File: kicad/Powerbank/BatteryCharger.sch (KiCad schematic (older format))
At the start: 48 parts, among them IC4 BQ25703ARSNT, Q4 Q_NMOS_GDS, Q5 Q_NMOS_GDS, Q8 Q_PMOS_GDS

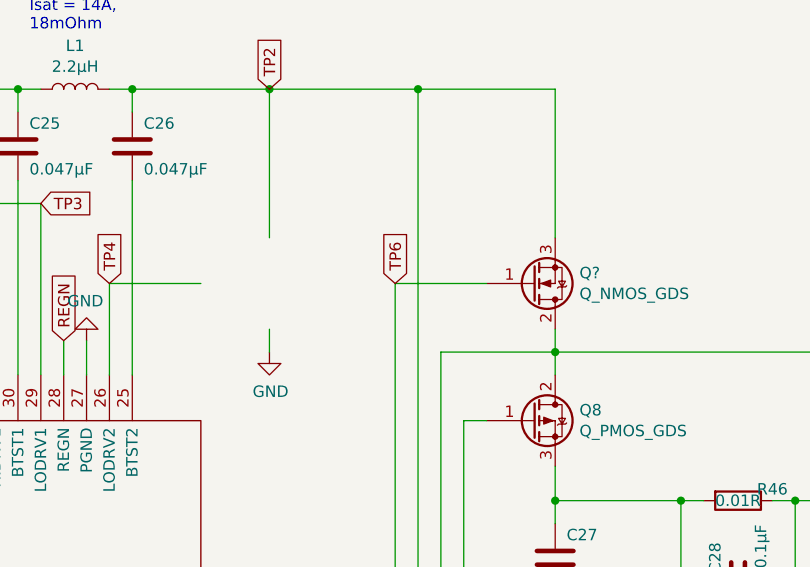
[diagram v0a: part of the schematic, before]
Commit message: Added more routing
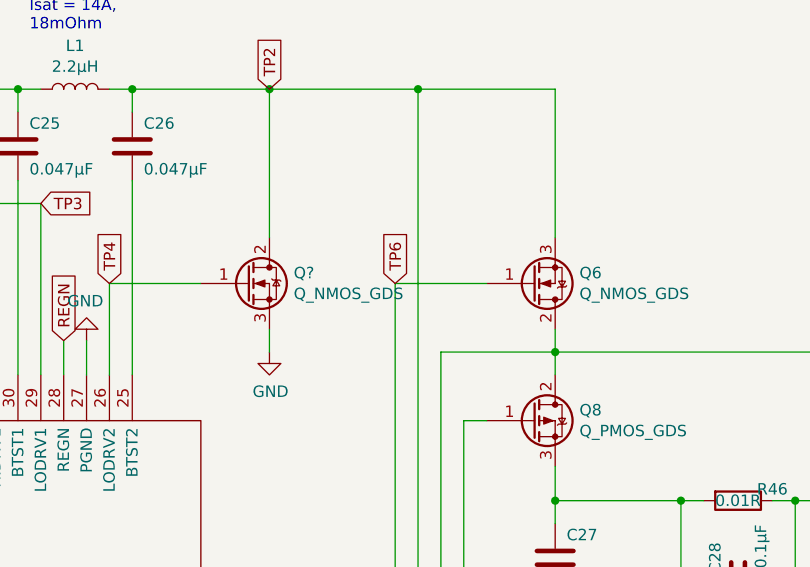
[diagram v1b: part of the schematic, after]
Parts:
- added Q?: Q_NMOS_GDS, Package_TO_SOT_SMD:TO-252-3_TabPin2, symbol Device:Q_NMOS_GDS
- gave numbers to parts that had none: 1
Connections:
- net GND: now also Q?.3 (S)
- net TP2: now also Q?.2 (D)
- net TP4: now also Q?.1 (G)
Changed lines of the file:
@@
+$EndComp
+$Comp
+L Device:Q_NMOS_GDS Q4
+U 1 1 5E148441
+P 4350 1700
+F 0 "Q4" V 4693 1700 50  0000 C CNN
+F 1 "Q_NMOS_GDS" V 4602 1700 50  0000 C CNN
+F 2 "Package_TO_SOT_SMD:TO-252-3_TabPin2" H 4550 1800 50  0001 C CNN
+F 3 "~" H 4350 1700 50  0001 C CNN
+	1    4350 1700
+	0    -1   -1   0
 $EndComp
 $Comp
@@
 $EndComp
 $Comp
-L Device:Q_NMOS_GDS Q4
-U 1 1 5E148441
-P 4350 1700
-F 0 "Q4" V 4693 1700 50  0000 C CNN
-F 1 "Q_NMOS_GDS" V 4602 1700 50  0000 C CNN
-F 2 "Package_TO_SOT_SMD:TO-252-3_TabPin2" H 4550 1800 50  0001 C CNN
-F 3 "~" H 4350 1700 50  0001 C CNN
-	1    4350 1700
-	0    -1   -1   0
-$EndComp
-$Comp
-L Device:Q_NMOS_GDS Q?
+L Device:Q_NMOS_GDS Q6
 U 1 1 5E20690D
 P 7850 2450
-F 0 "Q?" H 8056 2404 50  0000 L CNN
+F 0 "Q6" H 8056 2404 50  0000 L CNN
 F 1 "Q_NMOS_GDS" H 8056 2495 50  0000 L CNN
 F 2 "Package_TO_SOT_SMD:TO-252-3_TabPin2" H 8050 2550 50  0001 C CNN
@@
 	1    0    0    1
 $EndComp
+$Comp
+L Device:Q_NMOS_GDS Q?
+U 1 1 5E23DBD3
+P 6600 2450
+F 0 "Q?" H 6806 2496 50  0000 L CNN
+F 1 "Q_NMOS_GDS" H 6806 2405 50  0000 L CNN
+F 2 "Package_TO_SOT_SMD:TO-252-3_TabPin2" H 6800 2550 50  0001 C CNN
+F 3 "~" H 6600 2450 50  0001 C CNN
+	1    6600 2450
+	1    0    0    -1
+$EndComp
 $EndSCHEMATC

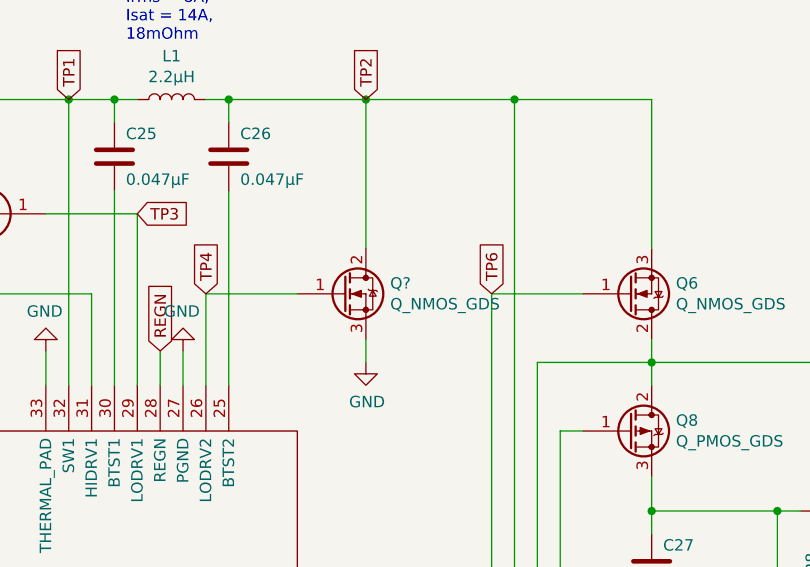
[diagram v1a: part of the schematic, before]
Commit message: Updated routing
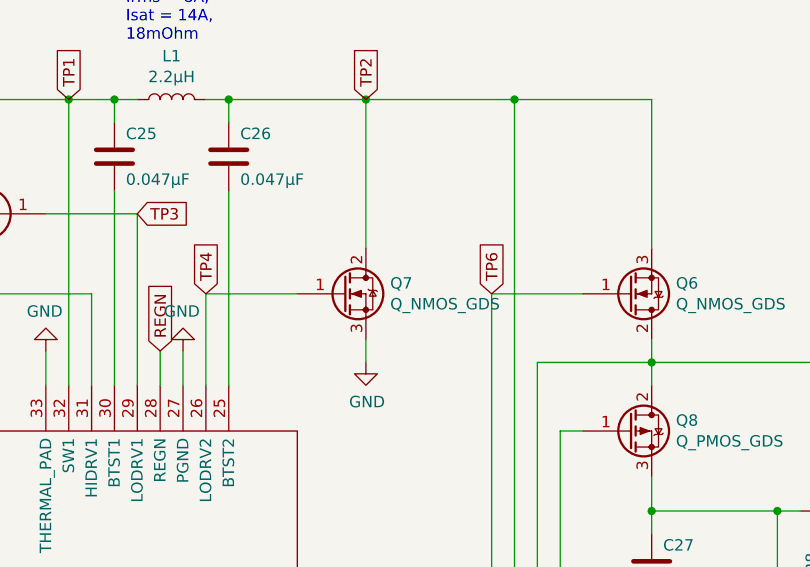
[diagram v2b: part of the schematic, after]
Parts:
- C12: footprint Capacitor_SMD:C_0603_1608Metric -> Capacitor_SMD:C_0805_2012Metric
- gave numbers to parts that had none: 1
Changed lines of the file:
@@
 F 0 "C12" H 1100 1750 50  0000 R CNN
 F 1 "22µF" H 1100 1950 50  0000 R CNN
-F 2 "Capacitor_SMD:C_0603_1608Metric" H 1188 1700 50  0001 C CNN
+F 2 "Capacitor_SMD:C_0805_2012Metric" H 1188 1700 50  0001 C CNN
 F 3 "~" H 1150 1850 50  0001 C CNN
 	1    1150 1850
@@
 $EndComp
 $Comp
-L Device:Q_NMOS_GDS Q?
+L Device:Q_NMOS_GDS Q7
 U 1 1 5E23DBD3
 P 6600 2450
-F 0 "Q?" H 6806 2496 50  0000 L CNN
+F 0 "Q7" H 6806 2496 50  0000 L CNN
 F 1 "Q_NMOS_GDS" H 6806 2405 50  0000 L CNN
 F 2 "Package_TO_SOT_SMD:TO-252-3_TabPin2" H 6800 2550 50  0001 C CNN

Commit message: Double checked footprint for IC and Mosfets
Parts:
- Q4, Q5, Q6, Q7: footprint Package_TO_SOT_SMD:TO-252-3_TabPin2 -> Package_TO_SOT_SMD:TO-252-2
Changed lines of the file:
@@
-$EndComp
-$Comp
-L Device:Q_NMOS_GDS Q4
-U 1 1 5E148441
-P 4350 1700
-F 0 "Q4" V 4693 1700 50  0000 C CNN
-F 1 "Q_NMOS_GDS" V 4602 1700 50  0000 C CNN
-F 2 "Package_TO_SOT_SMD:TO-252-3_TabPin2" H 4550 1800 50  0001 C CNN
-F 3 "~" H 4350 1700 50  0001 C CNN
-	1    4350 1700
-	0    -1   -1   0
-$EndComp
-$Comp
-L Device:Q_NMOS_GDS Q5
-U 1 1 5E13D30A
-P 5100 2100
-F 0 "Q5" H 5306 2146 50  0000 L CNN
-F 1 "Q_NMOS_GDS" H 5306 2055 50  0000 L CNN
-F 2 "Package_TO_SOT_SMD:TO-252-3_TabPin2" H 5300 2200 50  0001 C CNN
-F 3 "~" H 5100 2100 50  0001 C CNN
-	1    5100 2100
-	-1   0    0    -1
 $EndComp
 $Comp
@@
 F 0 "Q6" H 8056 2404 50  0000 L CNN
 F 1 "Q_NMOS_GDS" H 8056 2495 50  0000 L CNN
-F 2 "Package_TO_SOT_SMD:TO-252-3_TabPin2" H 8050 2550 50  0001 C CNN
+F 2 "Package_TO_SOT_SMD:TO-252-2" H 8050 2550 50  0001 C CNN
 F 3 "~" H 7850 2450 50  0001 C CNN
 	1    7850 2450
@@
 F 0 "Q7" H 6806 2496 50  0000 L CNN
 F 1 "Q_NMOS_GDS" H 6806 2405 50  0000 L CNN
-F 2 "Package_TO_SOT_SMD:TO-252-3_TabPin2" H 6800 2550 50  0001 C CNN
+F 2 "Package_TO_SOT_SMD:TO-252-2" H 6800 2550 50  0001 C CNN
 F 3 "~" H 6600 2450 50  0001 C CNN
 	1    6600 2450
 	1    0    0    -1
 $EndComp
+$Comp
+L Device:Q_NMOS_GDS Q5
+U 1 1 5E13D30A
+P 5100 2100
+F 0 "Q5" H 5306 2146 50  0000 L CNN
+F 1 "Q_NMOS_GDS" H 5306 2055 50  0000 L CNN
+F 2 "Package_TO_SOT_SMD:TO-252-2" H 5300 2200 50  0001 C CNN
+F 3 "~" H 5100 2100 50  0001 C CNN
+	1    5100 2100
+	-1   0    0    -1
+$EndComp
+$Comp
+L Device:Q_NMOS_GDS Q4
+U 1 1 5E148441
+P 4350 1700
+F 0 "Q4" V 4693 1700 50  0000 C CNN
+F 1 "Q_NMOS_GDS" V 4602 1700 50  0000 C CNN
+F 2 "Package_TO_SOT_SMD:TO-252-2" H 4550 1800 50  0001 C CNN
+F 3 "~" H 4350 1700 50  0001 C CNN
+	1    4350 1700
+	0    -1   -1   0
+$EndComp
 $EndSCHEMATC

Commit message: Updated layout in schematic for nicer look
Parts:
- renumbered C10 to C1, C19 to C10, C20 to C11, C21 to C12, C22 to C13, C23 to C14, C24 to C15, C25 to C16, C26 to C17, C27 to C18, C28 to C19, C11 to C2, C29 to C20, C30 to C21, C31 to C22, C32 to C23, C33 to C24, C34 to C25, C12 to C3, C13 to C4, C14 to C5, C15 to C6, C16 to C7, C17 to C8, C18 to C9, IC4 to IC1, Q4 to Q1, Q5 to Q2, Q7 to Q3, Q6 to Q4, Q8 to Q5, R33 to R10, R34 to R11, R35 to R12, R36 to R13, R37 to R14, R38 to R15, R39 to R16, R40 to R17, R41 to R18, R42 to R19, R43 to R20, R44 to R21, R45 to R22, R46 to R23, R47 to R24, R48 to R25, R32 to R9
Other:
- note added: "Buck-boost"
- note added: "Voltage from cell-balancer"
- note added: "Voltage to USB-PD controller"
